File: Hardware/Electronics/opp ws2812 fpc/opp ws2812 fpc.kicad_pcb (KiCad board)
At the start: 2 copper layers, 203 x 12 mm, 21 parts, among them J1 Conn_01x08

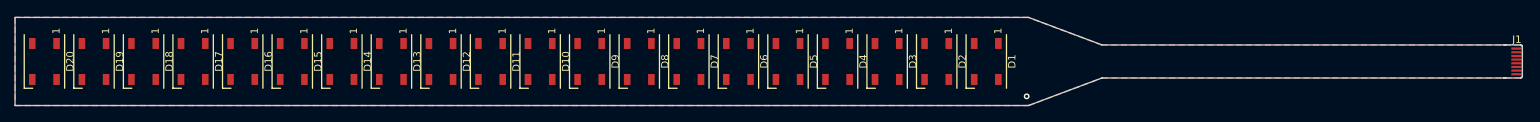
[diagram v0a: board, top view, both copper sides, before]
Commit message: Add 20 and 55 pixel strips
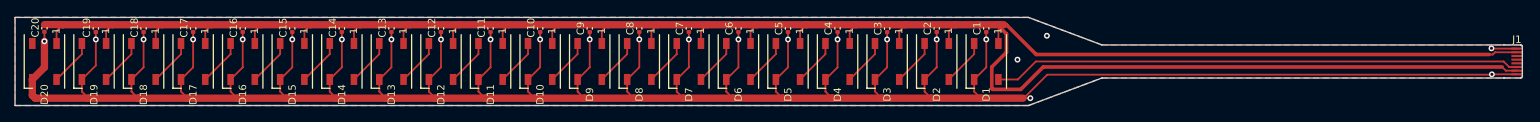
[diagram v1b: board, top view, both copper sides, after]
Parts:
- added C1: 100nf, Capacitor_SMD:C_0402_1005Metric, F.Cu at (152.2, 21.5)
- added C10: 100nf, Capacitor_SMD:C_0402_1005Metric, F.Cu at (91.5, 21.5)
- added C11: 100nf, Capacitor_SMD:C_0402_1005Metric, F.Cu at (84.8, 21.5)
- added C12: 100nf, Capacitor_SMD:C_0402_1005Metric, F.Cu at (78.0, 21.5)
- added C13: 100nf, Capacitor_SMD:C_0402_1005Metric, F.Cu at (71.2, 21.5)
- added C14: 100nf, Capacitor_SMD:C_0402_1005Metric, F.Cu at (64.5, 21.5)
- added C15: 100nf, Capacitor_SMD:C_0402_1005Metric, F.Cu at (57.8, 21.5)
- added C16: 100nf, Capacitor_SMD:C_0402_1005Metric, F.Cu at (51.0, 21.5)
- added C17: 100nf, Capacitor_SMD:C_0402_1005Metric, F.Cu at (44.2, 21.5)
- added C18: 100nf, Capacitor_SMD:C_0402_1005Metric, F.Cu at (37.5, 21.5)
- added C19: 100nf, Capacitor_SMD:C_0402_1005Metric, F.Cu at (31.0, 21.5)
- added C2: 100nf, Capacitor_SMD:C_0402_1005Metric, F.Cu at (145.5, 21.5)
- added C20: 100nf, Capacitor_SMD:C_0402_1005Metric, F.Cu at (24.0, 21.5)
- added C3: 100nf, Capacitor_SMD:C_0402_1005Metric, F.Cu at (138.8, 21.5)
- added C4: 100nf, Capacitor_SMD:C_0402_1005Metric, F.Cu at (132.0, 21.5)
- added C5: 100nf, Capacitor_SMD:C_0402_1005Metric, F.Cu at (125.2, 21.5)
- added C6: 100nf, Capacitor_SMD:C_0402_1005Metric, F.Cu at (118.5, 21.5)
- added C7: 100nf, Capacitor_SMD:C_0402_1005Metric, F.Cu at (111.8, 21.5)
- added C8: 100nf, Capacitor_SMD:C_0402_1005Metric, F.Cu at (105.0, 21.5)
- added C9: 100nf, Capacitor_SMD:C_0402_1005Metric, F.Cu at (98.2, 21.5)
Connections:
- D1 pad 4: Net-(D1-DIN) -> Data In
- J1 pad 3: Net-(D1-DIN) -> unconnected-(J1-Pin_3-Pad3)
- J1 pad 4: Net-(J1-Pin_4) -> unconnected-(J1-Pin_4-Pad4)
- J1 pad 5: Net-(J1-Pin_4) -> unconnected-(J1-Pin_5-Pad5)
- J1 pad 6: Net-(D1-DIN) -> Data In
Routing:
- net GND: track 0.00 -> 409.0 mm, vias 1 -> 25
- net +5V: track 0.00 -> 343.2 mm
- net Data In: track 0.00 -> 71.9 mm
- net Net-(D19-DOUT): track 0.00 -> 6.33 mm
- net Net-(D18-DOUT): track 0.00 -> 6.33 mm
- net Net-(D17-DOUT): track 0.00 -> 6.33 mm
- net Net-(D16-DOUT): track 0.00 -> 6.33 mm
- net Net-(D15-DOUT): track 0.00 -> 6.33 mm
- net Net-(D14-DOUT): track 0.00 -> 6.33 mm
- net Net-(D8-DOUT): track 0.00 -> 6.33 mm
- net Net-(D7-DOUT): track 0.00 -> 6.33 mm
- net Net-(D6-DOUT): track 0.00 -> 6.33 mm
- net Net-(D5-DOUT): track 0.00 -> 6.33 mm
- net Net-(D4-DOUT): track 0.00 -> 6.33 mm
- net Net-(D3-DOUT): track 0.00 -> 6.33 mm
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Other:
- board size 203 x 12 mm -> 202.8 x 12 mm
